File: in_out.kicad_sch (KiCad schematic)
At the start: 23 parts, among them J2 Conn_01x08, J3 Micro_SD_Card_Det1, Q3 NMOS, SW1 SW_Push, SW2 SW_Push, U6 DM-OLED096-636

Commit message: update pcb and schematic
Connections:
- net IO39: now also D5.1 (TVS1)
- net IO39_EXT: no longer D5.1 (TVS1)
- net IO40: now also D5.3 (TVS2)
- net IO40_EXT: no longer D5.3 (TVS2)
- net IO41: now also D5.4 (TVS3)
- net IO41_EXT: no longer D5.4 (TVS3)
- net IO42: now also D5.6 (TVS4)
- net IO42_EXT: no longer D5.6 (TVS4)
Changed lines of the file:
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@@
-	(wire
-		(pts
-			(xy 109.22 102.87) (xy 109.22 113.03)
-		)
-		(stroke
-			(width 0)
-			(type default)
-		)
-	)
 	(wire
 		(pts
@@
 	(wire
 		(pts
-			(xy 114.3 102.87) (xy 114.3 113.03)
-		)
-		(stroke
-			(width 0)
-			(type default)
-		)
-	)
-	(wire
-		(pts
 			(xy 163.83 83.82) (xy 165.1 83.82)
 		)
@@
 	(wire
 		(pts
-			(xy 106.68 102.87) (xy 106.68 113.03)
-		)
-		(stroke
-			(width 0)
-			(type default)
-		)
-	)
-	(wire
-		(pts
 			(xy 190.5 111.76) (xy 191.77 111.76)
 		)
@@
 	(wire
 		(pts
+			(xy 109.22 109.22) (xy 109.22 113.03)
+		)
+		(stroke
+			(width 0)
+			(type default)
+		)
+	)
+	(wire
+		(pts
 			(xy 162.56 111.76) (xy 172.72 111.76)
 		)
@@
 	(wire
 		(pts
+			(xy 116.84 109.22) (xy 116.84 113.03)
+		)
+		(stroke
+			(width 0)
+			(type default)
+		)
+	)
+	(wire
+		(pts
 			(xy 100.33 153.67) (xy 99.06 153.67)
 		)
@@
 	(wire
 		(pts
-			(xy 116.84 102.87) (xy 116.84 113.03)
-		)
-		(stroke
-			(width 0)
-			(type default)
-		)
-	)
-	(wire
-		(pts
 			(xy 207.01 143.51) (xy 208.28 143.51)
 		)
@@
 	(wire
 		(pts
+			(xy 106.68 109.22) (xy 106.68 113.03)
+		)
+		(stroke
+			(width 0)
+			(type default)
+		)
+	)
+	(wire
+		(pts
 			(xy 154.94 115.57) (xy 157.48 115.57)
 		)
@@
 		(pts
 			(xy 172.72 119.38) (xy 162.56 119.38)
+		)
+		(stroke
+			(width 0)
+			(type default)
+		)
+	)
+	(wire
+		(pts
+			(xy 114.3 109.22) (xy 114.3 113.03)
 		)
 		(stroke
@@
 	(label "RXD0_EXT"
 		(at 172.72 107.95 180)
-		(effects
-			(font
-				(size 1.27 1.27)
-			)
-			(justify right bottom)
-		)
-	)
-	(label "IO40_EXT"
-		(at 109.22 102.87 270)
-		(effects
-			(font
-				(size 1.27 1.27)
-			)
-			(justify right bottom)
-		)
-	)
-	(label "IO39_EXT"
-		(at 106.68 102.87 270)
-		(effects
-			(font
-				(size 1.27 1.27)
-			)
-			(justify right bottom)
-		)
-	)
-	(label "IO42_EXT"
-		(at 116.84 102.87 270)
-		(effects
-			(font
-				(size 1.27 1.27)
-			)
-			(justify right bottom)
-		)
-	)
-	(label "IO41_EXT"
-		(at 114.3 102.87 270)
 		(effects
 			(font
@@
 		)
 	)
+	(hierarchical_label "IO39"
+		(shape bidirectional)
+		(at 106.68 109.22 90)
+		(effects
+			(font
+				(size 1.27 1.27)
+			)
+			(justify left)
+		)
+	)
+	(hierarchical_label "IO42"
+		(shape bidirectional)
+		(at 116.84 109.22 90)
+		(effects
+			(font
+				(size 1.27 1.27)
+			)
+			(justify left)
+		)
+	)
 	(hierarchical_label "SD_DAT1"
 		(shape bidirectional)
@@
 		)
 	)
+	(hierarchical_label "IO41"
+		(shape bidirectional)
+		(at 114.3 109.22 90)
+		(effects
+			(font
+				(size 1.27 1.27)
+			)
+			(justify left)
+		)
+	)
 	(hierarchical_label "RGB_B"
 		(shape input)
@@
 		(effects
 			(font
+				(size 1.27 1.27)
+			)
+			(justify left)
+		)
+	)
+	(hierarchical_label "IO40"
+		(shape bidirectional)
+		(at 109.22 109.22 90)
+		(effects
+			(font

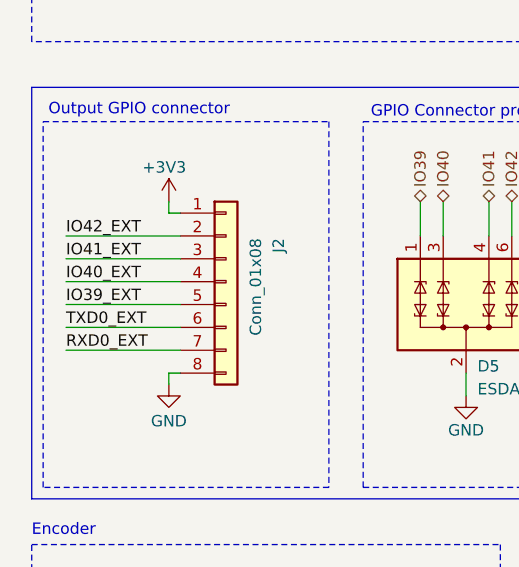
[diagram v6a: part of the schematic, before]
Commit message: change output connector pinout
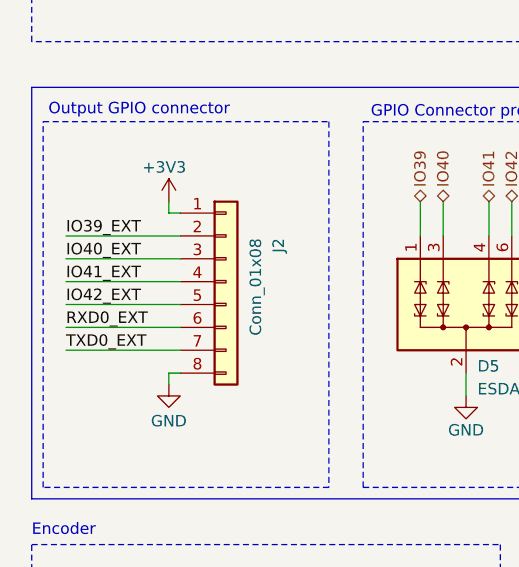
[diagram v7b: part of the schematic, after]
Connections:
- net IO39_EXT: now also J2.2 (Pin_2); no longer J2.5 (Pin_5)
- net IO40_EXT: now also J2.3 (Pin_3); no longer J2.4 (Pin_4)
- net IO41_EXT: now also J2.4 (Pin_4); no longer J2.3 (Pin_3)
- net IO42_EXT: now also J2.5 (Pin_5); no longer J2.2 (Pin_2)
- net RXD0_EXT: now also J2.6 (Pin_6); no longer J2.7 (Pin_7)
- net TXD0_EXT: now also J2.7 (Pin_7); no longer J2.6 (Pin_6)
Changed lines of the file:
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@@
 	)
 	(label "TXD0_EXT"
-		(at 67.31 123.19 0)
+		(at 67.31 125.73 0)
 		(effects
 			(font
@@
 	)
 	(label "IO40_EXT"
-		(at 67.31 118.11 0)
+		(at 67.31 115.57 0)
 		(effects
 			(font
@@
 	)
 	(label "IO42_EXT"
-		(at 67.31 113.03 0)
+		(at 67.31 120.65 0)
 		(effects
 			(font
@@
 	)
 	(label "RXD0_EXT"
-		(at 67.31 125.73 0)
+		(at 67.31 123.19 0)
 		(effects
 			(font
@@
 	)
 	(label "IO41_EXT"
-		(at 67.31 115.57 0)
+		(at 67.31 118.11 0)
 		(effects
 			(font
@@
 	)
 	(label "IO39_EXT"
-		(at 67.31 120.65 0)
+		(at 67.31 113.03 0)
 		(effects
 			(font

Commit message: finish routing
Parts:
- added JP1, JP2: SolderJumper_2_Open, Jumper:SolderJumper-2_P1.3mm_Open_TrianglePad1.0x1.5mm, symbol Jumper:SolderJumper_2_Open
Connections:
- net ENCODER_C: now also JP1.2 (B), JP2.2 (B); no longer U8.C
- net IO39: now also D5.6 (TVS4), R18.1; no longer D5.1 (TVS1), R15.1
- net IO39_EXT: now also R18.2; no longer R15.2
- net IO40: now also D5.4 (TVS3), R17.1; no longer D5.3 (TVS2), R16.1
- net IO40_EXT: now also R17.2; no longer R16.2
- net IO41: now also D5.3 (TVS2), R16.1; no longer D5.4 (TVS3), R17.1
- net IO41_EXT: now also R16.2; no longer R17.2
- net IO42: now also D5.1 (TVS1), R15.1; no longer D5.6 (TVS4), R18.1
- net IO42_EXT: now also R15.2; no longer R18.2
- net RXD0: now also D6.4 (TVS3), R14.1; no longer D6.6 (TVS4), R13.1
- net RXD0_EXT: now also R14.2; no longer R13.2
- net TXD0: now also D6.6 (TVS4), R13.1; no longer D6.4 (TVS3), R14.1
- net TXD0_EXT: now also R13.2; no longer R14.2
- new net: JP1.1 (A), JP2.1 (A), U8.C
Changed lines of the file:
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@@
 	(rectangle
 		(start 63.5 147.32)
-		(end 115.57 165.1)
+		(end 124.46 165.1)
 		(stroke
 			(width 0)
@@
 	)
 	(junction
+		(at 99.06 153.67)
+		(diameter 0)
+		(color 0 0 0 0)
+	)
+	(junction
 		(at 165.1 64.77)
 		(diameter 0)
@@
 	(wire
 		(pts
+			(xy 99.06 153.67) (xy 99.06 151.13)
+		)
+		(stroke
+			(width 0)
+			(type default)
+		)
+	)
+	(wire
+		(pts
 			(xy 172.72 127) (xy 162.56 127)
 		)
@@
 	(wire
 		(pts
-			(xy 100.33 153.67) (xy 99.06 153.67)
-		)
-		(stroke
-			(width 0)
-			(type default)
-		)
-	)
-	(wire
-		(pts
 			(xy 213.36 111.76) (xy 210.82 111.76)
 		)
@@
 	(wire
 		(pts
+			(xy 99.06 156.21) (xy 99.06 153.67)
+		)
+		(stroke
+			(width 0)
+			(type default)
+		)
+	)
+	(wire
+		(pts
 			(xy 190.5 111.76) (xy 190.5 106.68)
 		)
@@
 	(wire
 		(pts
+			(xy 110.49 151.13) (xy 110.49 156.21)
+		)
+		(stroke
+			(width 0)
+			(type default)
+		)
+	)
+	(wire
+		(pts
 			(xy 213.36 67.31) (xy 213.36 66.04)
 		)
@@
 	(wire
 		(pts
+			(xy 107.95 151.13) (xy 110.49 151.13)
+		)
+		(stroke
+			(width 0)
+			(type default)
+		)
+	)
+	(wire
+		(pts
 			(xy 82.55 158.75) (xy 83.82 158.75)
 		)
@@
 	(wire
 		(pts
+			(xy 100.33 156.21) (xy 99.06 156.21)
+		)
+		(stroke
+			(width 0)
+			(type default)
+		)
+	)
+	(wire
+		(pts
 			(xy 212.09 80.01) (xy 213.36 80.01)
 		)
@@
 	(wire
 		(pts
+			(xy 99.06 151.13) (xy 100.33 151.13)
+		)
+		(stroke
+			(width 0)
+			(type default)
+		)
+	)
+	(wire
+		(pts
 			(xy 66.04 66.04) (xy 68.58 66.04)
 		)
@@
 	(wire
 		(pts
+			(xy 107.95 156.21) (xy 110.49 156.21)
+		)
+		(stroke
+			(width 0)
+			(type default)
+		)
+	)
+	(wire
+		(pts
 			(xy 207.01 154.94) (xy 207.01 153.67)
 		)
@@
 	)
 	(label "IO39_EXT"
-		(at 172.72 115.57 180)
+		(at 172.72 127 180)
 		(effects
 			(font
@@
 	)
 	(label "IO41_EXT"
+		(at 172.72 119.38 180)
+		(effects
+			(font
+				(size 1.27 1.27)
+			)
+			(justify right bottom)
+		)
+	)
+	(label "IO40_EXT"
 		(at 172.72 123.19 180)
-		(effects
-			(font
-				(size 1.27 1.27)
-			)
-			(justify right bottom)
-		)
-	)
-	(label "IO40_EXT"
-		(at 172.72 119.38 180)
 		(effects
 			(font
@@
 	)
 	(label "IO42_EXT"
-		(at 172.72 127 180)
+		(at 172.72 115.57 180)
 		(effects
 			(font
@@
 	)
 	(label "TXD0_EXT"
-		(at 172.72 111.76 180)
+		(at 172.72 107.95 180)
 		(effects
 			(font
@@
 	)
 	(label "RXD0_EXT"
-		(at 172.72 107.95 180)
+		(at 172.72 111.76 180)
 		(effects
 			(font
@@
 	(hierarchical_label "RXD0"
 		(shape bidirectional)
-		(at 135.89 110.49 90)
+		(at 133.35 110.49 90)
 		(effects
 			(font
@@
 	(hierarchical_label "IO39"
 		(shape bidirectional)
-		(at 106.68 109.22 90)
+		(at 116.84 109.22 90)
 		(effects
 			(font
@@
 	(hierarchical_label "IO42"
 		(shape bidirectional)
-		(at 116.84 109.22 90)
+		(at 106.68 109.22 90)
 		(effects
 			(font
@@
 	(hierarchical_label "TXD0"
 		(shape bidirectional)
-		(at 133.35 110.49 90)
+		(at 135.89 110.49 90)
 		(effects
 			(font
@@
 	(hierarchical_label "IO41"
 		(shape bidirectional)
-		(at 114.3 109.22 90)
+		(at 109.22 109.22 90)
 		(effects
 			(font
@@
 	(hierarchical_label "ENCODER_C"
 		(shape input)
-		(at 100.33 153.67 0)
+		(at 110.49 153.67 0)
 		(effects
 			(font
@@
 	(hierarchical_label "IO39"
 		(shape bidirectional)
-		(at 154.94 115.57 180)
+		(at 154.94 127 180)
 		(effects
 			(font
@@
 	(hierarchical_label "RXD0"
 		(shape bidirectional)
-		(at 154.94 107.95 180)
+		(at 154.94 111.76 180)
 		(effects
 			(font
@@
 	(hierarchical_label "IO42"
 		(shape bidirectional)
-		(at 154.94 127 180)
+		(at 154.94 115.57 180)
 		(effects
 			(font
@@
 	(hierarchical_label "IO40"
 		(shape bidirectional)
-		(at 154.94 119.38 180)
+		(at 154.94 123.19 180)
 		(effects
 			(font
@@
 	(hierarchical_label "IO41"
 		(shape bidirectional)
-		(at 154.94 123.19 180)
+		(at 154.94 119.38 180)
 		(effects
 			(font
@@
 	(hierarchical_label "TXD0"
 		(shape bidirectional)
-		(at 154.94 111.76 180)
+		(at 154.94 107.95 180)
 		(effects
 			(font
@@
 	(hierarchical_label "IO40"
 		(shape bidirectional)
-		(at 109.22 109.22 90)
+		(at 114.3 109.22 90)
 		(effects
 			(font
@@
 				(path "/3130e1f2-bde1-4b12-bd54-0e1e50bd36da/1a9a8b3a-0ac6-451f-bc78-9d7f4c721b98"
 					(reference "R24")
+					(unit 1)
+				)
+			)
+		)
+	)
+	(symbol
+		(lib_id "Jumper:SolderJumper_2_Open")
+		(at 104.14 151.13 0)
+		(unit 1)
+		(exclude_from_sim no)
+		(in_bom no)
+		(on_board yes)
+		(dnp no)
+		(fields_autoplaced yes)
+		(property "Reference" "JP1"
+			(at 104.14 144.78 0)
+			(effects
+				(font
+					(size 1.27 1.27)
+				)
+			)
+		)
+		(property "Value" "SolderJumper_2_Open"
+			(at 104.14 147.32 0)
+			(effects
+				(font
+					(size 1.27 1.27)
+				)
+			)
+		)
+		(property "Footprint" "Jumper:SolderJumper-2_P1.3mm_Open_TrianglePad1.0x1.5mm"
+			(at 104.14 151.13 0)
+			(effects
+				(font
+					(size 1.27 1.27)
+				)
+				(hide yes)
+			)
+		)
+		(property "Datasheet" "~"
+			(at 104.14 151.13 0)
+			(effects
+				(font
+					(size 1.27 1.27)
+				)
+				(hide yes)
+			)
+		)
+		(property "Description" "Solder Jumper, 2-pole, open"
+			(at 104.14 151.13 0)
+			(effects
+				(font
+					(size 1.27 1.27)
+				)
+				(hide yes)
+			)
+		)
+		(pin "2"
+		)
+		(pin "1"
+		)
+		(instances
+			(project ""
+				(path "/3130e1f2-bde1-4b12-bd54-0e1e50bd36da/1a9a8b3a-0ac6-451f-bc78-9d7f4c721b98"
+					(reference "JP1")
 					(unit 1)
 				)
@@
 					(unit 1)
 				)
+			)
+		)
+	)
+	(symbol
+		(lib_id "Jumper:SolderJumper_2_Open")
+		(at 104.14 156.21 0)
+		(unit 1)
+		(exclude_from_sim no)
+		(in_bom no)
+		(on_board yes)
+		(dnp no)
+		(fields_autoplaced yes)
+		(property "Reference" "JP2"
+			(at 104.14 149.86 0)
+			(effects
+				(font
+					(size 1.27 1.27)
+				)
+			)
+		)
+		(property "Value" "SolderJumper_2_Open"
+			(at 104.14 152.4 0)
+			(effects
+				(font
+					(size 1.27 1.27)
+				)
+			)
+		)
+		(property "Footprint" "Jumper:SolderJumper-2_P1.3mm_Open_TrianglePad1.0x1.5mm"
+			(at 104.14 156.21 0)
+			(effects
+				(font
+					(size 1.27 1.27)
+				)
+				(hide yes)
+			)
+		)
+		(property "Datasheet" "~"
+			(at 104.14 156.21 0)
+			(effects
+				(font
+					(size 1.27 1.27)
+				)
+				(hide yes)
+			)
+		)
+		(property "Description" "Solder Jumper, 2-pole, open"
+			(at 104.14 156.21 0)
+			(effects
+				(font
+					(size 1.27 1.27)
+				)
+				(hide yes)
+			)
+		)
+		(pin "2"
+		)
+		(pin "1"
+		)
+		(instances
+			(project "pipu-zero"
+				(path "/3130e1f2-bde1-4b12-bd54-0e1e50bd36da/1a9a8b3a-0ac6-451f-bc78-9d7f4c721b98"
+					(reference "JP2")
+					(unit 1)
+				)
